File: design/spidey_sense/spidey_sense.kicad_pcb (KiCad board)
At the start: 2 copper layers, 57.5 x 37.5 mm, 24 parts, among them J1 Screw_Terminal_01x08, J2 Screw_Terminal_01x08, J3 Screw_Terminal_01x08, J4 Screw_Terminal_01x08, J5 Screw_Terminal_01x08, U1 LTC2984, U2 LM2931-5.0_SO8

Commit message: Add tracing
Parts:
- moved C1 10.7 mm to (124.7, 103.8)
- moved C5 8.15 mm to (128.5, 104.7), turned to 90 degrees
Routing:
- net /Sheet60AF3A60/R_sense: track 0.00 -> 62.6 mm, vias 0 -> 1
- net Net-(D1-Pad2): track 0.00 -> 44.9 mm, vias 0 -> 1
- net /sheet60B815B9/R_sense: track 0.00 -> 40.9 mm, vias 0 -> 1
- net +5V: track 0.00 -> 40.4 mm
- net /Sheet60AF3A60/conn_1: track 0.00 -> 34.2 mm
- net /sheet60B85CD9/conn_3: track 0.00 -> 32.1 mm
- net /Sheet60AF3A60/conn_2: track 0.00 -> 30.2 mm
- net /Sheet60AF3A60/conn_3: track 0.00 -> 27.5 mm
- net Net-(J1-Pad5): track 0.00 -> 27.3 mm
- net Net-(D4-Pad2): track 0.00 -> 27.2 mm, vias 0 -> 1
- net /sheet60B815B9/conn_3: track 0.00 -> 26.9 mm
- net /sheet60B85CD9/conn_2: track 0.00 -> 26.4 mm
- net GND: track 0.00 -> 24.3 mm, vias 0 -> 21
- net /sheet60B85CD9/conn_1: track 0.00 -> 24.3 mm
- net Net-(D2-Pad2): track 0.00 -> 24.0 mm, vias 0 -> 1
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- added copper zone on B.Cu, net GND
- added copper zone on F.Cu, net GND
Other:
- net class Default: clearance 0.2 -> 0.127
- rule trace_clearance: 0.2 -> 0.127

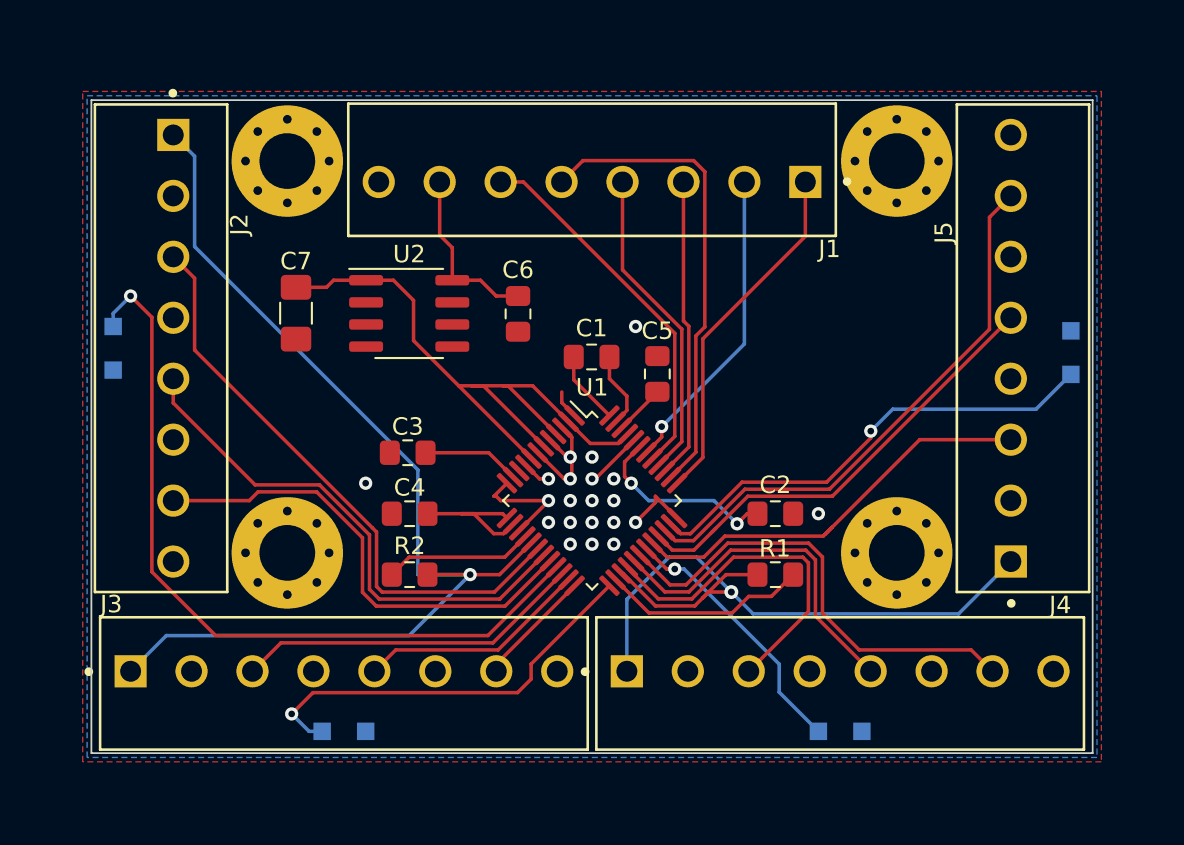
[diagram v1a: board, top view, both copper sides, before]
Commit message: Add silkscreen and gerbers
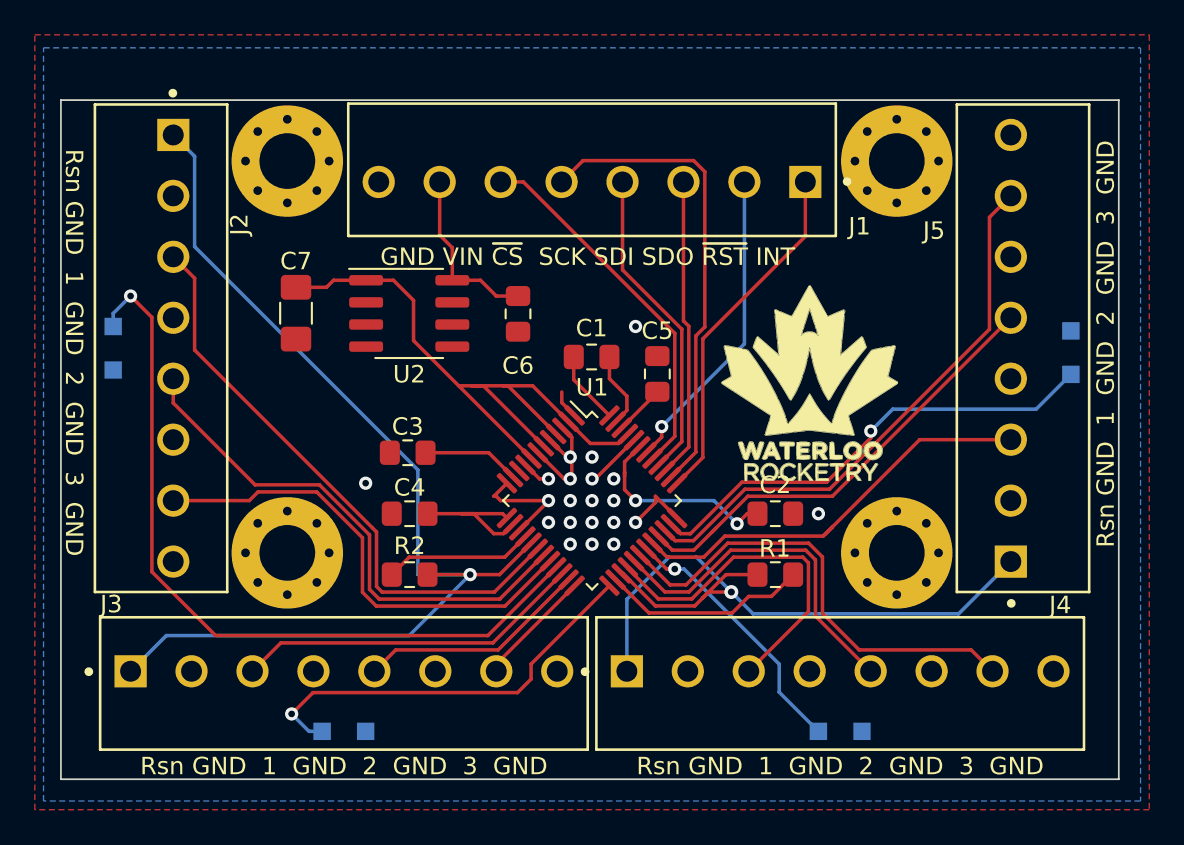
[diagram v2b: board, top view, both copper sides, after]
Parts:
- added G***: LOGO, footprints:spider_man, B.Cu at (124.2, 106.5)
- added G***: LOGO, footprints:logo, F.Cu at (137.2, 105.2)
- added G***: LOGO, footprints:logo, B.Cu at (107.5, 103.2)
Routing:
- net Net-(C2-Pad1): track 11.1 -> 11.8 mm
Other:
- board size 57.5 x 37.5 mm -> 60.8 x 39 mm
- board text added: "GND VIN ~CS~ SCK SDI SDO ~RST~ INT"
- board text added: "Rsn GND 1 GND 2 GND 3 GND"
- board text added: "SPIdey Sense Z.Mears 2021-05-26"

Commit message: Organized spidey_sense
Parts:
- removed D1, D2, D3, D4: D, Diode_SMD:D_SOD-323_HandSoldering
- removed G***: LOGO, footprints:spider_man
- removed G*** (x2): LOGO, footprints:logo
- removed the REF** at (142.2, 115.0)
- removed the REF** at (142.2, 92.5)
- removed the REF** at (107.2, 92.5)
- removed the REF** at (107.2, 115.0)
- added C10: 0.1uF, Capacitor_SMD:C_0805_2012Metric_Pad1.18x1.45mm_HandSolder, F.Cu at (90.5, 89.6)
- added C11: 0.1uF, Capacitor_SMD:C_0805_2012Metric_Pad1.18x1.45mm_HandSolder, F.Cu at (106.8, 86.1)
- added C8: 0.1uF, Capacitor_SMD:C_0805_2012Metric_Pad1.18x1.45mm_HandSolder, F.Cu at (90.5, 80.5)
- added C9: 0.1uF, Capacitor_SMD:C_0805_2012Metric_Pad1.18x1.45mm_HandSolder, F.Cu at (106.8, 77.0)
- added J6: Thermocouple_Terminal, TerminalBlock_Phoenix:TerminalBlock_Phoenix_MKDS-1,5-2-5.08_1x02_P5.08mm_Horizontal, F.Cu at (93.2, 101.9)
- added R3: 17.3kΩ, Resistor_SMD:R_0805_2012Metric_Pad1.20x1.40mm_HandSolder, F.Cu at (83.9, 80.8)
- added R4: 1kΩ, Resistor_SMD:R_0805_2012Metric_Pad1.20x1.40mm_HandSolder, F.Cu at (67.3, 86.4)
- added R5: 17.3kΩ, Resistor_SMD:R_0805_2012Metric_Pad1.20x1.40mm_HandSolder, F.Cu at (83.9, 89.9)
- added R6: 1kΩ, Resistor_SMD:R_0805_2012Metric_Pad1.20x1.40mm_HandSolder, F.Cu at (90.5, 77.2)
- added R7: 17.3kΩ, Resistor_SMD:R_0805_2012Metric_Pad1.20x1.40mm_HandSolder, F.Cu at (106.8, 80.8)
- added R8: 1kΩ, Resistor_SMD:R_0805_2012Metric_Pad1.20x1.40mm_HandSolder, F.Cu at (90.2, 86.4)
- added R9: 17.3kΩ, Resistor_SMD:R_0805_2012Metric_Pad1.20x1.40mm_HandSolder, F.Cu at (106.8, 90.0)
- added REF**: MountingHole_3.2mm_M3_Pad, MountingHole:MountingHole_3.2mm_M3_Pad, F.Cu at (50.8, 66.6)
- added REF**: MountingHole_3.2mm_M3_Pad, MountingHole:MountingHole_3.2mm_M3_Pad, F.Cu at (105.8, 101.6)
- added REF**: MountingHole_3.2mm_M3_Pad, MountingHole:MountingHole_3.2mm_M3_Pad, F.Cu at (50.8, 101.6)
- added REF**: MountingHole_3.2mm_M3_Pad, MountingHole:MountingHole_3.2mm_M3_Pad, F.Cu at (105.8, 66.6)
- added TP1: TestPoint, TestPoint:TestPoint_Pad_1.5x1.5mm, F.Cu at (61.7, 77.7)
- added U3: LT1001, Package_SO:SOP-8_3.9x4.9mm_P1.27mm, F.Cu at (76.1, 87.9)
- added U4: LT1001, Package_SO:SOP-8_3.9x4.9mm_P1.27mm, F.Cu at (76.1, 78.8)
- added U5: LT1001, Package_SO:SOP-8_3.9x4.9mm_P1.27mm, F.Cu at (99.0, 78.8)
- added U6: LT1001, Package_SO:SOP-8_3.9x4.9mm_P1.27mm, F.Cu at (99.0, 87.9)
- C1, C2: value 10uF -> 0.1uF; footprint Capacitor_SMD:C_0805_2012Metric_Pad1.15x1.40mm_HandSolder -> Capacitor_SMD:C_0805_2012Metric_Pad1.18x1.45mm_HandSolder
- C3: value 0.1uF -> 10uF; footprint Capacitor_SMD:C_0805_2012Metric_Pad1.15x1.40mm_HandSolder -> Capacitor_SMD:C_0805_2012Metric_Pad1.18x1.45mm_HandSolder
- C4: value 1uF -> 10uF; footprint Capacitor_SMD:C_0805_2012Metric_Pad1.15x1.40mm_HandSolder -> Capacitor_SMD:C_0805_2012Metric_Pad1.18x1.45mm_HandSolder
- C5: value 10uF -> 1uF; footprint Capacitor_SMD:C_0805_2012Metric_Pad1.15x1.40mm_HandSolder -> Capacitor_SMD:C_0805_2012Metric_Pad1.18x1.45mm_HandSolder
- C6: footprint Capacitor_SMD:C_0805_2012Metric_Pad1.15x1.40mm_HandSolder -> Capacitor_SMD:C_0805_2012Metric_Pad1.18x1.45mm_HandSolder
- C7: value 100uF -> 0.1uF; footprint Capacitor_SMD:C_1206_3216Metric_Pad1.42x1.75mm_HandSolder -> Capacitor_SMD:C_0805_2012Metric_Pad1.18x1.45mm_HandSolder
- J1: value Screw_Terminal_01x08 -> Input_Screw_Terminal; footprint footprints:Phoenix_Contact-1984675-0-0-0 -> TerminalBlock_Phoenix:TerminalBlock_Phoenix_MKDS-1,5-2-5.08_1x02_P5.08mm_Horizontal
- J2: value Screw_Terminal_01x08 -> Output_Screw_Terminal; footprint footprints:Phoenix_Contact-1984675-0-0-0 -> TerminalBlock_Phoenix:TerminalBlock_Phoenix_MKDS-1,5-4-5.08_1x04_P5.08mm_Horizontal
- J3, J4, J5: value Screw_Terminal_01x08 -> Thermocouple_Terminal; footprint footprints:Phoenix_Contact-1984675-0-0-0 -> TerminalBlock_Phoenix:TerminalBlock_Phoenix_MKDS-1,5-2-5.08_1x02_P5.08mm_Horizontal
- R1: value 10K -> 150kΩ; footprint Resistor_SMD:R_0805_2012Metric_Pad1.15x1.40mm_HandSolder -> Resistor_SMD:R_0805_2012Metric_Pad1.20x1.40mm_HandSolder
- R2: value 10K -> 1kΩ; footprint Resistor_SMD:R_0805_2012Metric_Pad1.15x1.40mm_HandSolder -> Resistor_SMD:R_0805_2012Metric_Pad1.20x1.40mm_HandSolder
- U1: value LTC2984 -> LT1025; footprint Package_QFP:LQFP-48_7x7mm_P0.5mm -> Package_SO:SOP-8_3.9x4.9mm_P1.27mm
- U2: value LM2931-5.0_SO8 -> LTC1983-5; footprint Package_SO:SOIC-8_3.9x4.9mm_P1.27mm -> Package_SO:TSOP-6_1.65x3.05mm_P0.95mm
- moved C5 82.0 mm to (49.7, 82.0), turned to -90 degrees
- moved R1 79.2 mm to (61.2, 88.4), turned to 90 degrees
- moved U1 76.6 mm to (51.6, 89.2), turned to 0 degrees
- moved J4 72.2 mm to (69.8, 101.9)
- moved J5 68.0 mm to (81.5, 101.9), turned to 0 degrees
- moved C3 67.8 mm to (55.1, 75.9), turned to -90 degrees
- moved U2 62.8 mm to (54.4, 81.9), turned to -90 degrees
- moved C4 61.3 mm to (61.0, 82.5), turned to 0 degrees
- moved R2 60.8 mm to (67.6, 77.2)
- moved C1 58.8 mm to (67.7, 89.6)
- moved C2 57.9 mm to (84.0, 86.0)
- moved C6 56.8 mm to (67.7, 80.5), turned to 0 degrees
- moved J3 56.2 mm to (58.2, 101.9)
- moved J1 47.6 mm to (85.1, 66.6)
- moved J2 45.3 mm to (73.4, 66.6), turned to 180 degrees
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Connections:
- C1 pad 1: Net-(C1-Pad1) -> /Amplifier2/K+
- C1 pad 2: Net-(C1-Pad2) -> GND
- C2 pad 1: Net-(C2-Pad1) -> /Amplifier2/Vout
- C2 pad 2: GND -> Net-(C2-Pad2)
- C3 pad 1: Net-(C3-Pad1) -> +5V
- C4 pad 1: Net-(C4-Pad1) -> -5V
- C5 pad 2: GND -> Net-(C5-Pad2)
- C6 pad 1: Net-(C6-Pad1) -> /Amplifier1/K+
- C7 pad 1: +5V -> /Amplifier1/Vout
- C7 pad 2: GND -> Net-(C7-Pad2)
- J1 pad 1: Net-(J1-Pad1) -> GND
- J1 pad 2: Net-(J1-Pad2) -> +5V
- J2 pad 1: /Sheet60AF3A60/R_sense -> /Amplifier4/Vout
- J2 pad 2: GND -> /Amplifier3/Vout
- J2 pad 3: /Sheet60AF3A60/conn_1 -> /Amplifier2/Vout
- J2 pad 4: GND -> /Amplifier1/Vout
- J3 pad 1: /Sheet60AF3A60/R_sense -> /K-
- J3 pad 2: GND -> /Amplifier1/K+
- J4 pad 1: /sheet60B815B9/R_sense -> /K-
- J4 pad 2: GND -> /Amplifier2/K+
- J5 pad 1: /sheet60B815B9/R_sense -> /K-
- J5 pad 2: GND -> /Amplifier3/K+
- R1 pad 2: /sheet60B815B9/R_sense -> -5V
- R2 pad 1: Net-(R2-Pad1) -> GND
- R2 pad 2: /Sheet60AF3A60/R_sense -> Net-(C7-Pad2)
- U1 pad 1: GND -> unconnected-(U1-Pad1)
- U1 pad 3: GND -> Net-(R1-Pad1)
- U1 pad 4: +5V -> GND
- U1 pad 6: +5V -> unconnected-(U1-Pad6)
- U1 pad 7: GND -> /K-
- U1 pad 8: +5V -> unconnected-(U1-Pad8)
- U2 pad 2: GND -> -5V
- U2 pad 3: GND -> Net-(C5-Pad1)
- U2 pad 4: Net-(U2-Pad4) -> Net-(C5-Pad2)
- U2 pad 5: Net-(U2-Pad5) -> GND
- U2 pad 6: GND -> +5V
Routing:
- net +5V: track 40.4 -> 179.1 mm, vias 0 -> 2
- net -5V: track 0.00 -> 111.9 mm
- net /K-: track 0.00 -> 80.6 mm
- net /Sheet60AF3A60/R_sense: track 62.6 -> 0.00 mm, vias 1 -> 0
- net /Amplifier3/Vout: track 0.00 -> 55.0 mm, vias 0 -> 1
- net /Amplifier4/Vout: track 0.00 -> 54.9 mm, vias 0 -> 1
- net Net-(D1-Pad2): track 44.9 -> 0.00 mm, vias 1 -> 0
- net /sheet60B815B9/R_sense: track 40.9 -> 0.00 mm, vias 1 -> 0
- net Net-(C7-Pad2): track 0.00 -> 40.5 mm
- net Net-(C9-Pad2): track 0.00 -> 39.4 mm
- net Net-(C2-Pad2): track 0.00 -> 39.3 mm
- net /Amplifier2/Vout: track 0.00 -> 37.5 mm, vias 0 -> 1
- net Net-(C11-Pad2): track 0.00 -> 35.2 mm
- net /Amplifier3/K+: track 0.00 -> 34.6 mm, vias 0 -> 1
- net /Amplifier1/K+: track 0.00 -> 34.6 mm, vias 0 -> 1
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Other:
- board size 60.8 x 39 mm -> 63.5 x 46.5 mm
- net class Default removed
- rule pad_to_mask_clearance: 0.05 -> 0
- board text added: "+5V"
- board text added: "GND"
- board text added: "K+"
- board text added: "K-"
- board text added: "LOW ESR"
- board text added: "V3"
- board text added: "V4"
- board text added: "V5"
- board text added: "V6"
- board text removed: "GND VIN ~CS~ SCK SDI SDO ~RST~ INT"
- board text removed: "Rsn GND 1 GND 2 GND 3 GND"
- board text removed: "SPIdey Sense Z.Mears 2021-05-26"

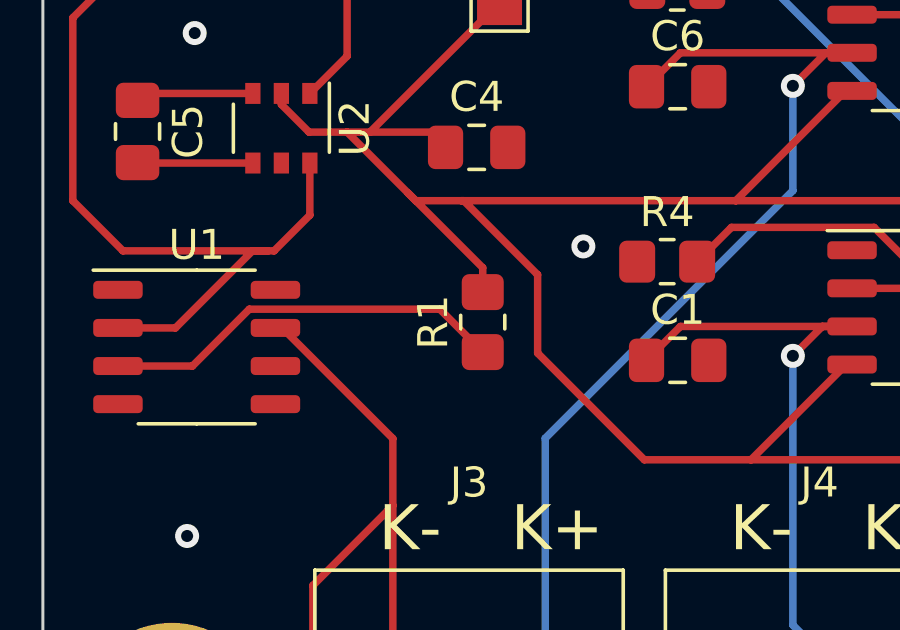
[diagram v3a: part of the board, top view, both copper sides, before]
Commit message: Added vias to avoid GND loops
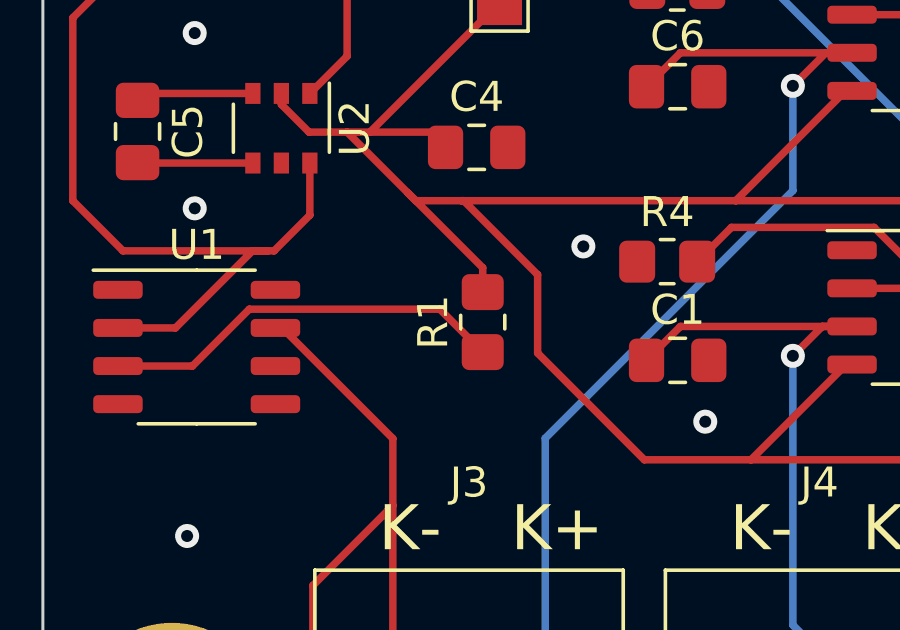
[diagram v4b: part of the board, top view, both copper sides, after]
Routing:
- net GND: vias 6 -> 8
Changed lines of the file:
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@@
   (via (at 64.262 76.2) (size 0.8) (drill 0.4) (layers "F.Cu" "B.Cu") (free) (net 2))
   (via (at 64.516 85.852) (size 0.8) (drill 0.4) (layers "F.Cu" "B.Cu") (free) (net 2))
+  (via (at 51.562 84.582) (size 0.8) (drill 0.4) (layers "F.Cu" "B.Cu") (free) (net 2))
   (via (at 87.884 91.44) (size 0.8) (drill 0.4) (layers "F.Cu" "B.Cu") (free) (net 2))
+  (via (at 68.58 91.694) (size 0.8) (drill 0.4) (layers "F.Cu" "B.Cu") (free) (net 2))
   (via (at 51.562 78.74) (size 0.8) (drill 0.4) (layers "F.Cu" "B.Cu") (free) (net 2))
   (via (at 51.308 95.504) (size 0.8) (drill 0.4) (layers "F.Cu" "B.Cu") (free) (net 2))

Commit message: Initial schematic design
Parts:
- removed C1, C10, C11, C2, C6, C7, C8, C9: 0.1uF, Capacitor_SMD:C_0805_2012Metric_Pad1.18x1.45mm_HandSolder
- removed C3, C4: 10uF, Capacitor_SMD:C_0805_2012Metric_Pad1.18x1.45mm_HandSolder
- removed C5: 1uF, Capacitor_SMD:C_0805_2012Metric_Pad1.18x1.45mm_HandSolder
- removed R1: 150kΩ, Resistor_SMD:R_0805_2012Metric_Pad1.20x1.40mm_HandSolder
- removed R2, R4, R6, R8: 1kΩ, Resistor_SMD:R_0805_2012Metric_Pad1.20x1.40mm_HandSolder
- removed R3, R5, R7, R9: 17.3kΩ, Resistor_SMD:R_0805_2012Metric_Pad1.20x1.40mm_HandSolder
- removed REF** (x4): MountingHole_3.2mm_M3_Pad, MountingHole:MountingHole_3.2mm_M3_Pad
- removed TP1: TestPoint, TestPoint:TestPoint_Pad_1.5x1.5mm
- removed U1: LT1025, Package_SO:SOP-8_3.9x4.9mm_P1.27mm
- removed U2: LTC1983-5, Package_SO:TSOP-6_1.65x3.05mm_P0.95mm
- removed U3, U4, U5, U6: LT1001, Package_SO:SOP-8_3.9x4.9mm_P1.27mm
- added J6: Conn_01x06_Female, Connector_PinSocket_2.54mm:PinSocket_1x06_P2.54mm_Vertical, F.Cu at (71.1, 90.2)
- added J7: Conn_01x06_Female, Connector_PinSocket_2.54mm:PinSocket_1x06_P2.54mm_Vertical, F.Cu at (82.5, 90.1)
- added J8: Conn_01x06_Female, Connector_PinSocket_2.54mm:PinSocket_1x06_P2.54mm_Vertical, F.Cu at (95.2, 90.2)
- added J9: Conn_01x06_Female, Connector_PinSocket_2.54mm:PinSocket_1x06_P2.54mm_Vertical, F.Cu at (58.4, 90.2)
- moved J4 0.26 mm to (81.3, 101.9)
- renumbered J2 to J10, J3 to J2, J4 to J3, J5 to J4, J6 to J5
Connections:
- J1 pad 2: +5V -> +24V
- J10 pad 1: /Amplifier4/Vout -> Net-(J8-Pad5)
- J10 pad 2: /Amplifier3/Vout -> Net-(J7-Pad5)
- J10 pad 3: /Amplifier2/Vout -> Net-(J6-Pad5)
- J10 pad 4: /Amplifier1/Vout -> Net-(J10-Pad4)
- J2 pad 1: /K- -> Net-(J2-Pad1)
- J2 pad 2: /Amplifier1/K+ -> Net-(J2-Pad2)
- J3 pad 1: /K- -> Net-(J3-Pad1)
- J3 pad 2: /Amplifier2/K+ -> Net-(J3-Pad2)
- J4 pad 1: /K- -> Net-(J4-Pad1)
- J4 pad 2: /Amplifier3/K+ -> Net-(J4-Pad2)
- J5 pad 1: /K- -> Net-(J5-Pad1)
- J5 pad 2: /Amplifier4/K+ -> Net-(J5-Pad2)
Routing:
- net +5V: track 179.1 -> 0.00 mm, vias 2 -> 0
- net -5V: track 111.9 -> 0.00 mm
- net /K-: track 80.6 -> 0.00 mm
- net /Amplifier3/Vout: track 55.0 -> 0.00 mm, vias 1 -> 0
- net /Amplifier4/Vout: track 54.9 -> 0.00 mm, vias 1 -> 0
- net Net-(C7-Pad2): track 40.5 -> 0.00 mm
- net Net-(C9-Pad2): track 39.4 -> 0.00 mm
- net Net-(C2-Pad2): track 39.3 -> 0.00 mm
- net /Amplifier2/Vout: track 37.5 -> 0.00 mm, vias 1 -> 0
- net Net-(C11-Pad2): track 35.2 -> 0.00 mm
- net /Amplifier3/K+: track 34.6 -> 0.00 mm, vias 1 -> 0
- net /Amplifier1/K+: track 34.6 -> 0.00 mm, vias 1 -> 0
- net /Amplifier1/Vout: track 34.5 -> 0.00 mm
- net Net-(J8-Pad5): track 0.00 -> 29.2 mm
- net /Amplifier4/K+: track 24.2 -> 0.00 mm, vias 1 -> 0
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- added copper zone on F.Cu, net +24V
- removed copper zone on F.Cu, net GND
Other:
- board text removed: "+5V"
- board text removed: "GND"
- board text removed: "K+"
- board text removed: "K-"
- board text removed: "LOW ESR"
- board text removed: "V3"
- board text removed: "V4"
- board text removed: "V5"
- board text removed: "V6"
